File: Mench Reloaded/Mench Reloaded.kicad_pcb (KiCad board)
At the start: 2 copper layers, 160 x 100 mm, 56 parts, among them IC1 DS1813, J1 FTDI serial, J2 Conn_01x40_Pin, J3 RAM CSB select, J4 Conn_01x40_Pin, J5 Barrel_Jack_Switch, SW1 SW_Push, U1 W65C265SxQ, U2 128K RAM, U3 28C256, U4 LM7805_TO220, U5 74HC00, Y1 32.768 kHz, Y2 3.6864 mHz

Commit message: Completed initial PCB layout. Commiting because I will try to reduce it to 100mm x 100mm
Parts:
- U4: footprint Package_TO_SOT_THT:TO-220-3_Vertical -> Package_TO_SOT_THT:TO-220-3_Horizontal_TabDown
- moved R9 39.7 mm to (173.4, 96.5), turned to 180 degrees
- moved D5 33.4 mm to (166.0, 96.5), turned to 180 degrees
- moved C1 18.1 mm to (128.0, 119.0), turned to 0 degrees
- moved Y1 15.2 mm to (127.0, 113.6), turned to 90 degrees
- moved C3 13.9 mm to (128.0, 106.0), turned to 0 degrees
- moved R1 9.24 mm to (119.0, 106.0), turned to 180 degrees
- moved RN1 7.62 mm to (75.3, 109.4)
- moved R4 6.59 mm to (131.2, 91.7), turned to 90 degrees
- moved D8 6.21 mm to (178.0, 129.0)
- moved R12 6.16 mm to (178.0, 135.0)
- moved R2 5.68 mm to (130.2, 96.7)
- moved Y2 5.50 mm to (138.8, 91.9)
- moved D7 4.27 mm to (173.0, 129.0)
- moved R11 4.11 mm to (173.0, 135.0)
- moved R3 4.08 mm to (120.0, 112.6), turned to -90 degrees
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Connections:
- R3 pad 1: Net-(U1-~{CLKO}) -> Net-(C3-Pad1)
- R4 pad 1: Net-(U1-~{FCLKO}) -> Net-(C4-Pad1)
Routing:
- net +5V: track 21.3 -> 0.00 mm
- net Net-(D4-K): track 3.25 -> 0.00 mm
- net Net-(D3-K): track 3.22 -> 0.00 mm
- net Net-(D1-K): track 3.14 -> 0.00 mm
- net Net-(D6-K): track 3.10 -> 0.00 mm
- net Net-(D8-K): track 3.03 -> 0.00 mm
- net Net-(D7-K): track 3.07 -> 0.13 mm
- net Net-(D5-K): track 3.14 -> 0.38 mm
- net Net-(D2-K): track 3.18 -> 0.51 mm

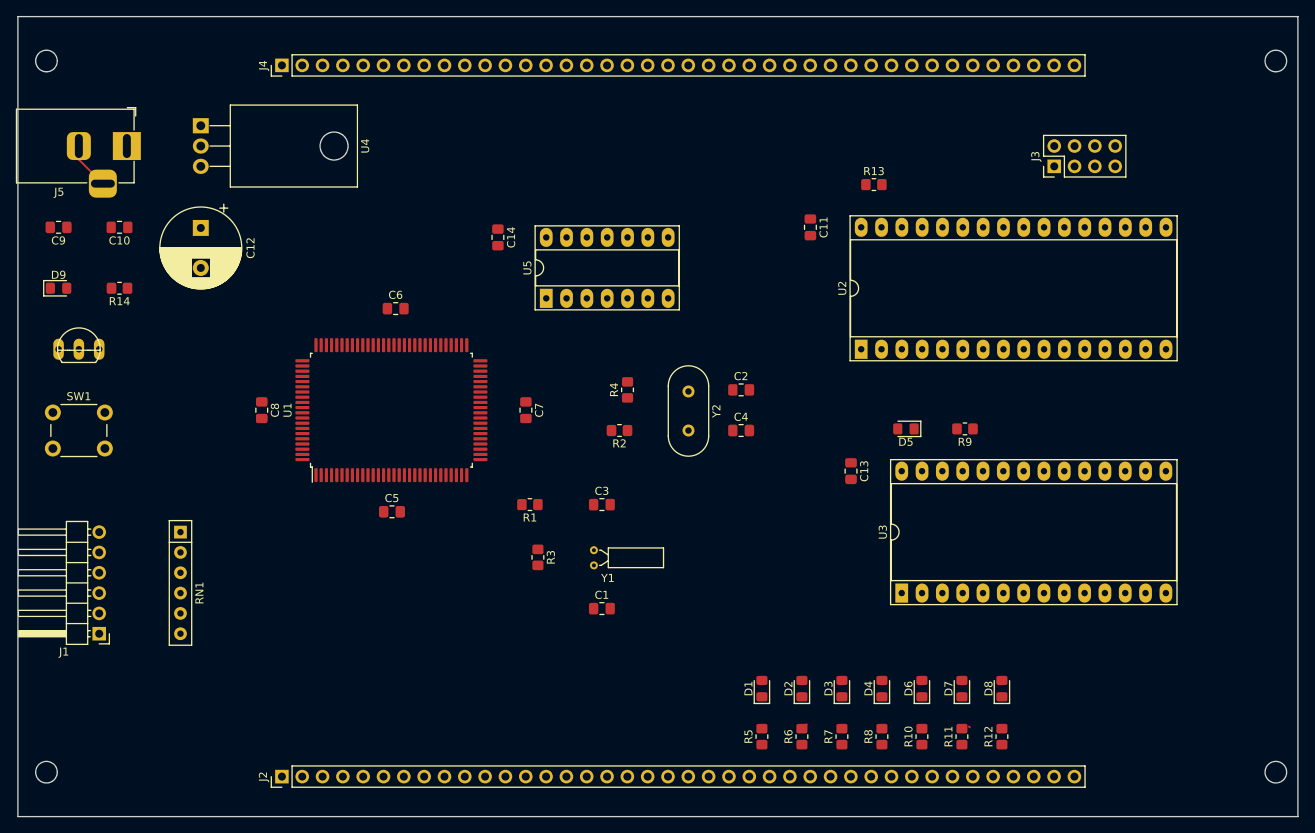
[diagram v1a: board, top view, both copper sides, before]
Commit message: Reworked the layout to 100mm by 100mm. Also changed the headers to be compatible with the W65C265SXB.
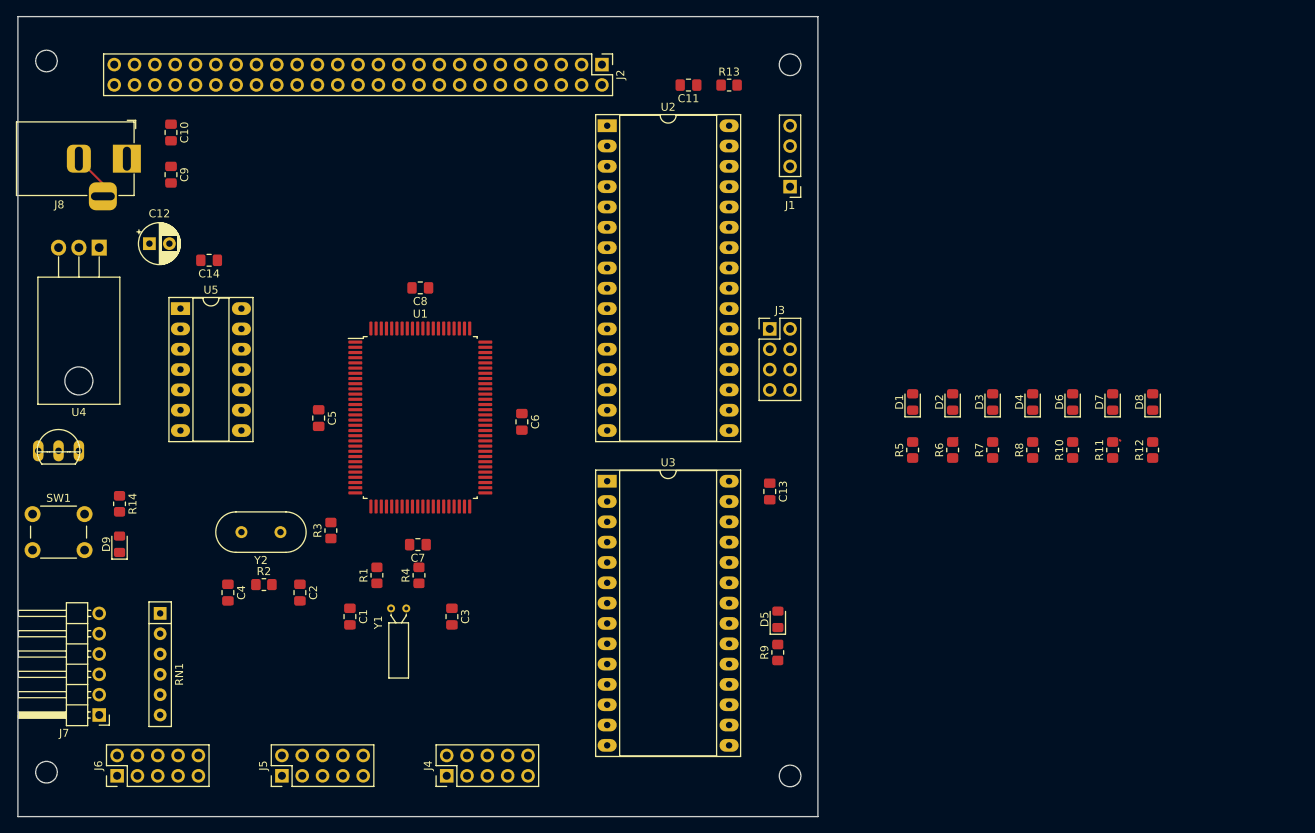
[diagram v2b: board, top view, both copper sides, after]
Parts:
- added J1: TGx, Connector_PinHeader_2.54mm:PinHeader_1x04_P2.54mm_Vertical, F.Cu at (151.5, 66.3)
- added J5: P5x, Connector_PinHeader_2.54mm:PinHeader_2x05_P2.54mm_Vertical, F.Cu at (88.0, 139.9)
- added J6: P6x, Connector_PinHeader_2.54mm:PinHeader_2x05_P2.54mm_Vertical, F.Cu at (67.4, 139.9)
- C12: footprint Capacitor_THT:CP_Radial_D10.0mm_P5.00mm -> Capacitor_THT:CP_Radial_D5.0mm_P2.50mm
- J2: value Conn_01x40_Pin -> XBUS_265; footprint Connector_PinHeader_2.54mm:PinHeader_1x40_P2.54mm_Vertical -> Connector_PinHeader_2.54mm:PinHeader_2x25_P2.54mm_Vertical
- J4: value Conn_01x40_Pin -> P4x; footprint Connector_PinHeader_2.54mm:PinHeader_1x40_P2.54mm_Vertical -> Connector_PinHeader_2.54mm:PinHeader_2x05_P2.54mm_Vertical
- moved J2 97.6 mm to (128.0, 51.0), turned to -90 degrees
- moved J4 91.2 mm to (108.6, 139.9)
- moved C4 67.3 mm to (81.2, 117.0), turned to -90 degrees
- moved MH3 60.7 mm to (151.5, 51.0)
- moved MH4 60.7 mm to (151.5, 139.9)
- moved C2 60.7 mm to (90.2, 117.0), turned to -90 degrees
- moved Y2 53.9 mm to (87.8, 109.4), turned to 180 degrees
- moved R2 51.6 mm to (85.8, 116.0), turned to 0 degrees
- moved U5 45.7 mm to (75.3, 81.5), turned to 0 degrees
- moved U2 42.3 mm to (128.7, 58.6), turned to 0 degrees
- moved J3 41.0 mm to (149.0, 84.0), turned to 0 degrees
- moved D1 40.5 mm to (166.8, 93.2)
- moved D2 40.5 mm to (171.8, 93.2)
- moved D3 40.5 mm to (176.8, 93.2)
- moved D4 40.5 mm to (181.8, 93.2)
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- renumbered J1 to J7, J5 to J8, R3 to R1, R4 to R2, R2 to R3, R1 to R4
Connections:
- J2 pad 10: a0 -> d7
- J2 pad 11: a1 -> a0
- J2 pad 12: a2 -> a1
- J2 pad 13: a3 -> a2
- J2 pad 14: a4 -> a3
- J2 pad 15: a5 -> a4
- J2 pad 16: a6 -> a5
- J2 pad 17: a7 -> a6
- J2 pad 18: a8 -> a7
- J2 pad 19: a9 -> a8
- J2 pad 2: d0 -> GND
- J2 pad 20: a10 -> a9
- J2 pad 21: a11 -> a10
- J2 pad 22: a12 -> a11
- J2 pad 23: a13 -> a12
- J2 pad 24: a14 -> a13
- J2 pad 25: a15 -> a14
- J2 pad 26: csb0 -> a15
- J2 pad 27: csb1 -> a16
- J2 pad 28: csb2 -> a17
- J2 pad 29: csb3 -> a18
- J2 pad 3: d1 -> d0
- J2 pad 30: csb5 -> a19
- J2 pad 31: csb6 -> a20
- J2 pad 32: csb7 -> a21
- J2 pad 33: NMIB -> a22
- J2 pad 34: IRQB -> a23
- J2 pad 35: RESB -> csb0
- J2 pad 36: PHI2 -> csb1
- J2 pad 37: WEB -> csb5
- J2 pad 38: MEMWEB -> csb6
- J2 pad 39: MEMOEB -> csb7
- J2 pad 4: d2 -> d1
- J2 pad 40: GND -> IRQB
- J2 pad 5: d3 -> d2
- J2 pad 6: d4 -> d3
- J2 pad 7: d5 -> d4
- J2 pad 8: d6 -> d5
- J2 pad 9: d7 -> d6
- J4 pad 10: DTRB0 -> PIRS2
- J4 pad 2: a16 -> GND
- J4 pad 3: a17 -> NMIB
- J4 pad 4: a18 -> IRQB
- J4 pad 5: a19 -> PIIB
- J4 pad 6: a20 -> FA15
- J4 pad 7: a21 -> AMS
- J4 pad 8: a22 -> PIRS0
- J4 pad 9: a23 -> PIRS1
- R3 pad 2: Net-(U1-~{FCLKO}) -> FCLKOB
- R4 pad 2: Net-(U1-~{CLKO}) -> CLKOB
- U1 pad 33: Net-(U1-~{FCLKO}) -> FCLKOB
- U1 pad 37: Net-(U1-~{CLKO}) -> CLKOB
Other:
- board size 160 x 100 mm -> 100 x 100 mm

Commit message: Increased the vertical spacing of the components. Aligned the 0-volt pins of the RAM and ROM. Made sure that no resistors or diodes are in the parallel feed area. Removed the unused chip select indicator diodes. I can add them to any cards that use the expansion header. Moved the interrupt select header and diode above the 65c22 because that area was available. For the 65c22 chip I used a5b for cs1 and cs1b for cs2b. This should map it to 0xDFC0.
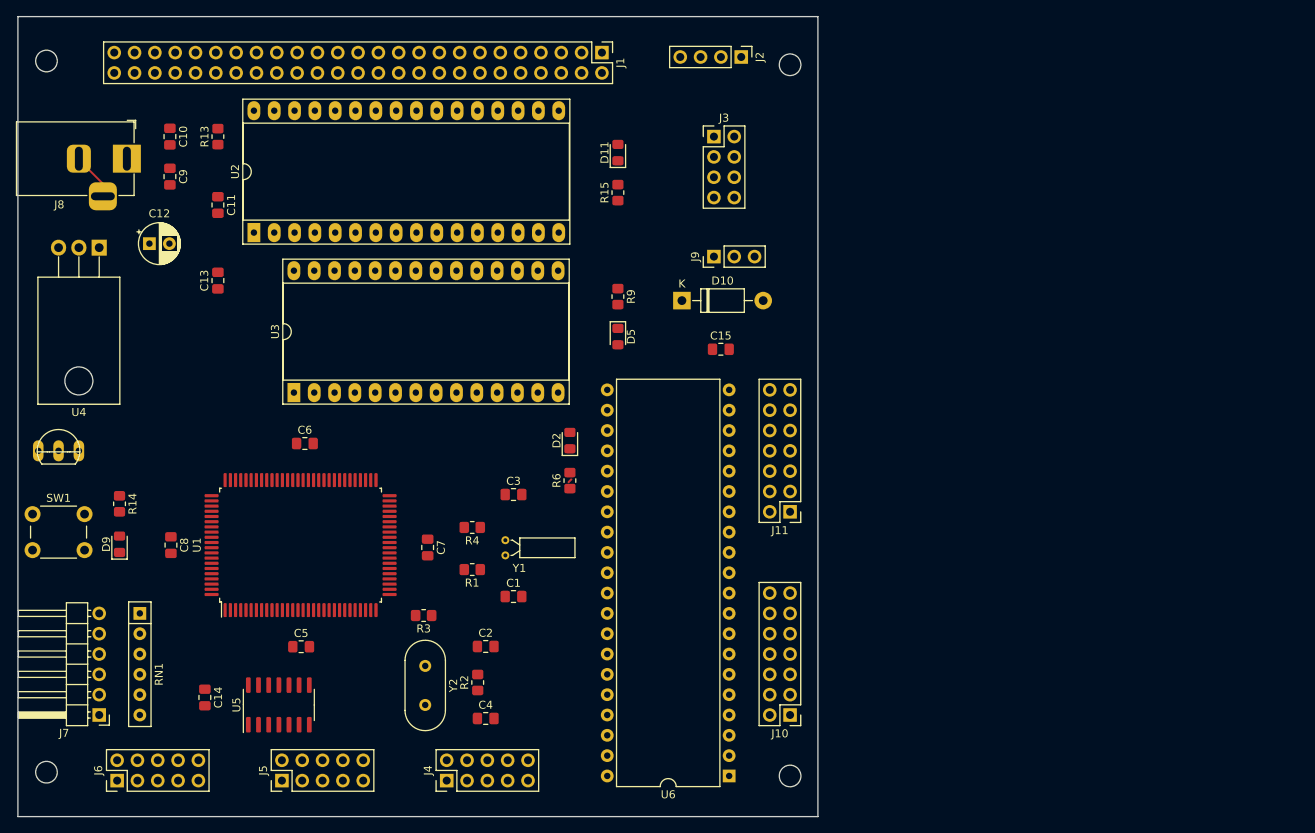
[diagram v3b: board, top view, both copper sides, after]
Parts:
- removed D1, D3, D4, D6, D7, D8: green, LED_SMD:LED_0805_2012Metric_Pad1.15x1.40mm_HandSolder
- removed R10, R11, R12, R5, R7, R8: 3K, Resistor_SMD:R_0805_2012Metric_Pad1.20x1.40mm_HandSolder
- added C15: 0.1uF, Capacitor_SMD:C_0805_2012Metric_Pad1.18x1.45mm_HandSolder, F.Cu at (142.9, 86.6)
- added D10: 1N5817, Diode_THT:D_DO-41_SOD81_P10.16mm_Horizontal, F.Cu at (138.0, 80.5)
- added D11: green, LED_SMD:LED_0805_2012Metric_Pad1.15x1.40mm_HandSolder, F.Cu at (130.0, 62.0)
- added J10: VIA1 Port A, Connector_PinHeader_2.54mm:PinHeader_2x07_P2.54mm_Vertical, F.Cu at (151.5, 132.3)
- added J11: VIA1 Port B, Connector_PinHeader_2.54mm:PinHeader_2x07_P2.54mm_Vertical, F.Cu at (151.5, 106.9)
- added J9: Int Sel 1, Connector_PinHeader_2.54mm:PinHeader_1x03_P2.54mm_Vertical, F.Cu at (142.0, 75.0)
- added R15: 3K, Resistor_SMD:R_0805_2012Metric_Pad1.20x1.40mm_HandSolder, F.Cu at (130.0, 67.0)
- added U6: W65C22SxP, Package_DIP:DIP-40_W15.24mm, F.Cu at (143.9, 139.9)
- J8: value Barrel_Jack_Switch -> DC Power
- U5: footprint Package_DIP:DIP-14_W7.62mm_Socket_LongPads -> Package_SO:SOIC-14_3.9x8.7mm_P1.27mm
- moved C13 73.8 mm to (80.0, 78.0), turned to 90 degrees
- moved R13 64.2 mm to (80.0, 60.0), turned to 90 degrees
- moved C11 60.7 mm to (80.0, 68.5), turned to -90 degrees
- moved C14 54.7 mm to (78.4, 130.1), turned to -90 degrees
- moved U5 51.0 mm to (87.6, 131.0), turned to 90 degrees
- moved R9 48.8 mm to (130.0, 80.0), turned to -90 degrees
- moved D2 48.1 mm to (124.0, 98.0)
- moved R6 48.0 mm to (124.0, 103.0)
- moved U2 46.1 mm to (84.5, 72.0), turned to 90 degrees
- moved C8 44.8 mm to (74.1, 111.1), turned to -90 degrees
- moved U3 40.7 mm to (89.5, 92.0), turned to 90 degrees
- moved D5 40.6 mm to (130.0, 85.0), turned to -90 degrees
- moved C4 35.9 mm to (113.5, 132.7), turned to 0 degrees
- moved R2 29.4 mm to (112.5, 128.2), turned to 90 degrees
- moved C5 28.7 mm to (90.4, 123.8), turned to 0 degrees
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- renumbered J2 to J1, J1 to J2
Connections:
- J3 pad 2: Net-(J3-Pin_1) -> csb3
- J3 pad 4: Net-(J3-Pin_1) -> csb5
- J3 pad 5: csb7 -> Net-(J3-Pin_1)
- J3 pad 7: csb5 -> Net-(J3-Pin_1)
- J3 pad 8: csb3 -> csb7

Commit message: Reworked the schematic to aid with routing. Began routing the pcb.
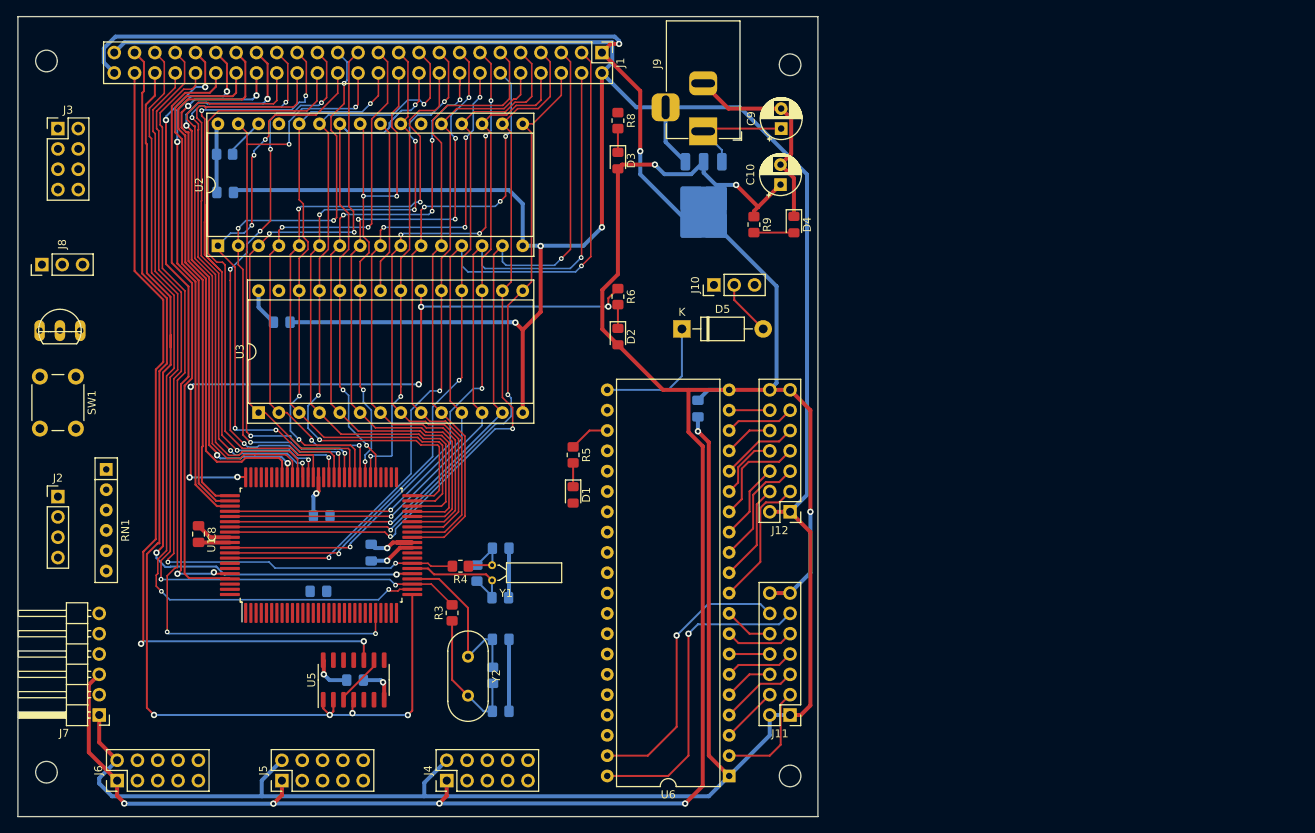
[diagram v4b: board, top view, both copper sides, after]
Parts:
- removed the C10 at (74.0, 60.0)
- removed D11: green, LED_SMD:LED_0805_2012Metric_Pad1.15x1.40mm_HandSolder
- removed R13, R15: 3K, Resistor_SMD:R_0805_2012Metric_Pad1.20x1.40mm_HandSolder
- added D3: green, LED_SMD:LED_0805_2012Metric_Pad1.15x1.40mm_HandSolder, F.Cu at (130.0, 63.0)
- added J8: EEPROM R/W, Connector_PinHeader_2.54mm:PinHeader_1x03_P2.54mm_Vertical, F.Cu at (58.0, 76.0)
- added R7: 3K, Resistor_SMD:R_0805_2012Metric_Pad1.20x1.40mm_HandSolder, B.Cu at (80.8, 62.2)
- added R8: 3K, Resistor_SMD:R_0805_2012Metric_Pad1.20x1.40mm_HandSolder, F.Cu at (130.0, 58.0)
- C1, C11, C2, C3, C4, C5, C6, C7, R1, R2: moved to B.Cu
- C10: renamed from C12; value 10uF -> 100uF
- C12: renamed from C13; moved to B.Cu
- C13: renamed from C14; moved to B.Cu
- C14: renamed from C15; moved to B.Cu
- C9: value 0.33uF -> 10uF; footprint Capacitor_SMD:C_0805_2012Metric_Pad1.18x1.45mm_HandSolder -> Capacitor_THT:CP_Radial_D5.0mm_P2.50mm
- U1: footprint Package_QFP:PQFP-100_14x20mm_P0.65mm -> Mench Reloaded_footprints:PQFP-100_14x20mm_P0.65mm_HandSolder
- U2: value 128K RAM -> 68c128 SRAM; footprint Package_DIP:DIP-32_W15.24mm_Socket_LongPads -> Package_DIP:DIP-32_W15.24mm_Socket
- U3: footprint Package_DIP:DIP-28_W15.24mm_Socket_LongPads -> Package_DIP:DIP-28_W15.24mm_Socket
- U4: value LM7805_TO220 -> LM1117 TO-252-3; footprint Package_TO_SOT_THT:TO-220-3_Horizontal_TabDown -> Package_TO_SOT_SMD:TO-252-3_TabPin2; moved to B.Cu
- moved J2 101.6 mm to (60.0, 105.0), turned to 0 degrees
- moved D4 93.3 mm to (152.0, 71.0), turned to -90 degrees
- moved R9 86.6 mm to (147.0, 71.0)
- moved J3 82.0 mm to (60.0, 59.0)
- moved C10 79.2 mm to (150.3, 66.0), turned to 90 degrees
- moved C9 76.6 mm to (150.4, 59.0), turned to 90 degrees
- moved U4 75.8 mm to (140.7, 68.2), turned to -90 degrees
- moved J9 72.1 mm to (140.7, 59.3), turned to -90 degrees
- moved C13 18.9 mm to (97.1, 127.9), turned to 0 degrees
- moved RN1 18.5 mm to (66.0, 101.6)
- moved SW1 18.0 mm to (62.2, 90.0), turned to -90 degrees
- moved IC1 15.0 mm to (60.2, 84.2)
- moved U5 9.87 mm to (97.0, 127.9)
- moved C12 9.52 mm to (88.0, 83.2), turned to 0 degrees
- moved C6 9.29 mm to (93.0, 107.4)
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- renumbered D2 to D1, D5 to D2, D9 to D4, D10 to D5, J9 to J10, J10 to J11, J11 to J12, J8 to J9, R6 to R5, R9 to R6, R14 to R9
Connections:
- net Net-(J3-Pin_1) renamed MEMCS1B
- U2 pad 1: unconnected-(U2-NC-Pad1) -> a17
- U2 pad 30: Net-(U2-CS2) -> MEMCS2
- U3 pad 27: MEMWEB -> Net-(J8-Pin_2)
- U4 pad 1: Net-(U4-VI) -> GND
- U4 pad 2: GND -> +5V
- U4 pad 3: +5V -> Net-(U4-VI)
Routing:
- net GND: track 5.94 -> 520.3 mm, vias 0 -> 6
- net +5V: track 0.00 -> 415.5 mm, vias 0 -> 12
- net WEB: track 0.00 -> 139.5 mm, vias 0 -> 4
- net FCLKOB: track 0.00 -> 104.4 mm, vias 0 -> 2
- net PHI2: track 0.00 -> 104.3 mm, vias 0 -> 2
- net CLKOB: track 0.00 -> 103.9 mm, vias 0 -> 2
- net d0: track 0.00 -> 103.8 mm, vias 0 -> 2
- net RUN: track 0.00 -> 103.6 mm, vias 0 -> 2
- net RESB: track 0.00 -> 103.4 mm, vias 0 -> 2
- net d1: track 0.00 -> 98.3 mm, vias 0 -> 2
- net d2: track 0.00 -> 98.2 mm, vias 0 -> 2
- net BE: track 0.00 -> 97.6 mm, vias 0 -> 2
- net d4: track 0.00 -> 94.4 mm, vias 0 -> 2
- net a7: track 0.00 -> 91.2 mm, vias 0 -> 2
- net d6: track 0.00 -> 90.9 mm, vias 0 -> 2
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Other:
- board text removed: "Mounting holes are optional Keepout areas are for for guide rails"

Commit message: Rerouting XBUS and related
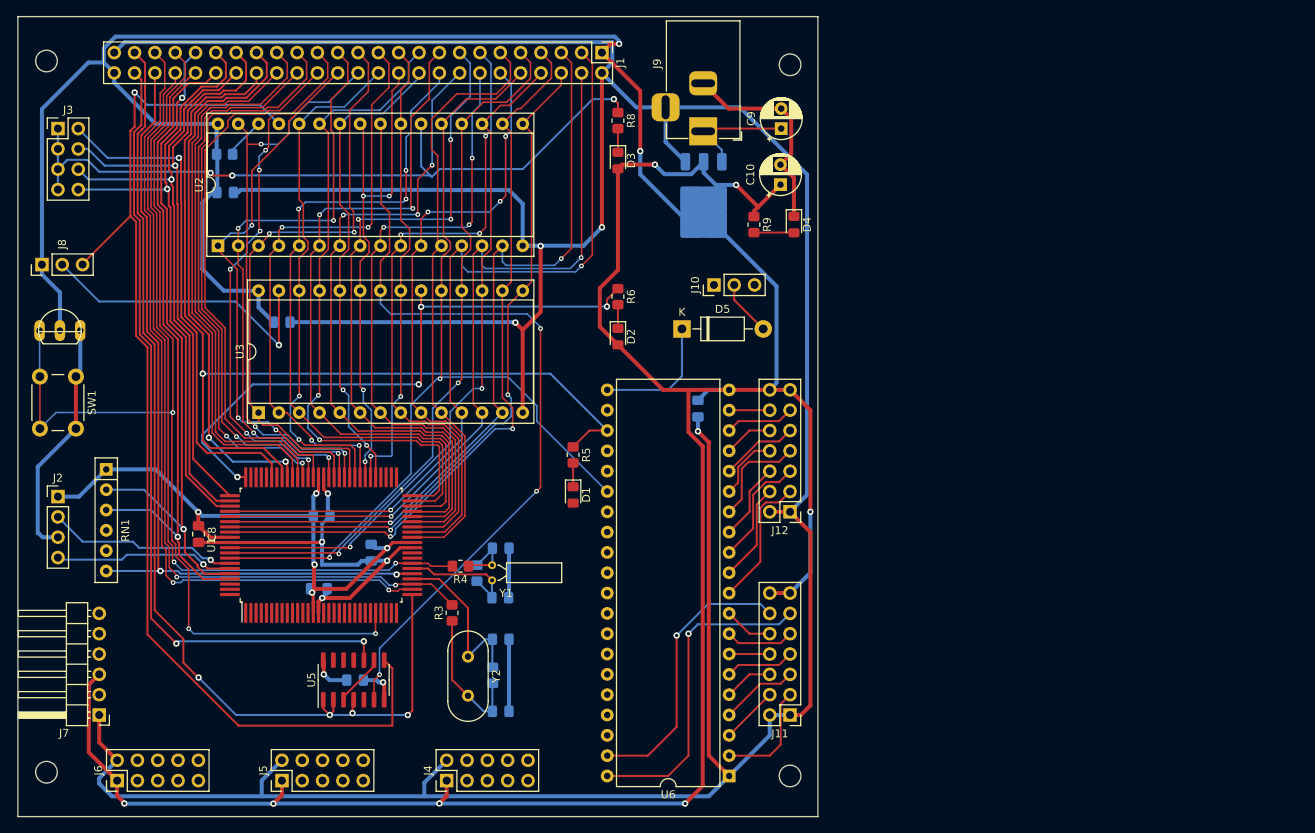
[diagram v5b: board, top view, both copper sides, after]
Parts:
- moved C5 0.33 mm to (92.6, 116.5)
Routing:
- net MEMWEB: track 0.00 -> 141.2 mm, vias 0 -> 1
- net +5V: track 415.5 -> 549.7 mm, vias 12 -> 15
- net MEMCS1B: track 0.00 -> 91.4 mm, vias 0 -> 3
- net MEMOEB: track 21.8 -> 100.0 mm, vias 0 -> 3
- net GND: track 520.3 -> 593.8 mm, vias 6 -> 9
- net csb3: track 0.00 -> 62.8 mm, vias 0 -> 1
- net csb1: track 74.3 -> 124.4 mm, vias 2 -> 1
- net Net-(J8-Pin_2): track 0.00 -> 38.1 mm, vias 0 -> 1
- net d7: track 88.2 -> 114.5 mm
- net RESB: track 103.4 -> 129.5 mm, vias 2 -> 3
- net TG0: track 0.00 -> 23.9 mm, vias 0 -> 1
- net TG1: track 0.00 -> 22.6 mm, vias 0 -> 1
- net a9: track 72.6 -> 59.8 mm, vias 3 -> 2
- net a20: track 85.0 -> 72.4 mm, vias 4 -> 2
- net csb7: track 65.9 -> 77.5 mm, vias 2 -> 1
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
